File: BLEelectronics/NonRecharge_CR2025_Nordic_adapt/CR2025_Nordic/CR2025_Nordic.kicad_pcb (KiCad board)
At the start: 2 copper layers, 24 parts, among them J1 USB_A_PLUG, J2 AU-Y1006-R, Q1 Si2307CDS, U1 TPD2E2U06, U2 BAT-HLD-001, U3 LTC4412xS6, U4 LTC4054LES5-4.2#TRPBF, U5 AT25SF081-XMHD-X

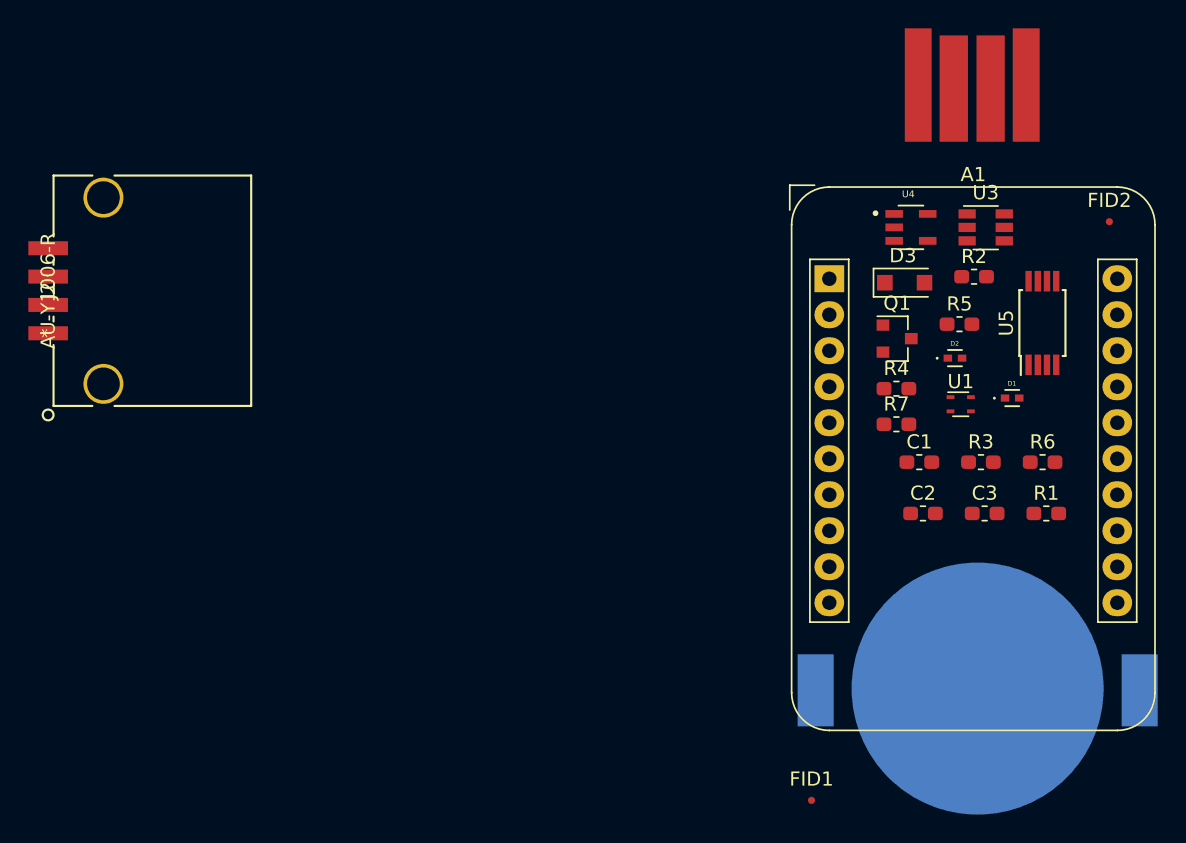
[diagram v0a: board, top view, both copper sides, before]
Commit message: added LP5970 .3V regulator to 5USB input. Created custom Nordic nRF52840 header. Todo: layout and pack libraries.
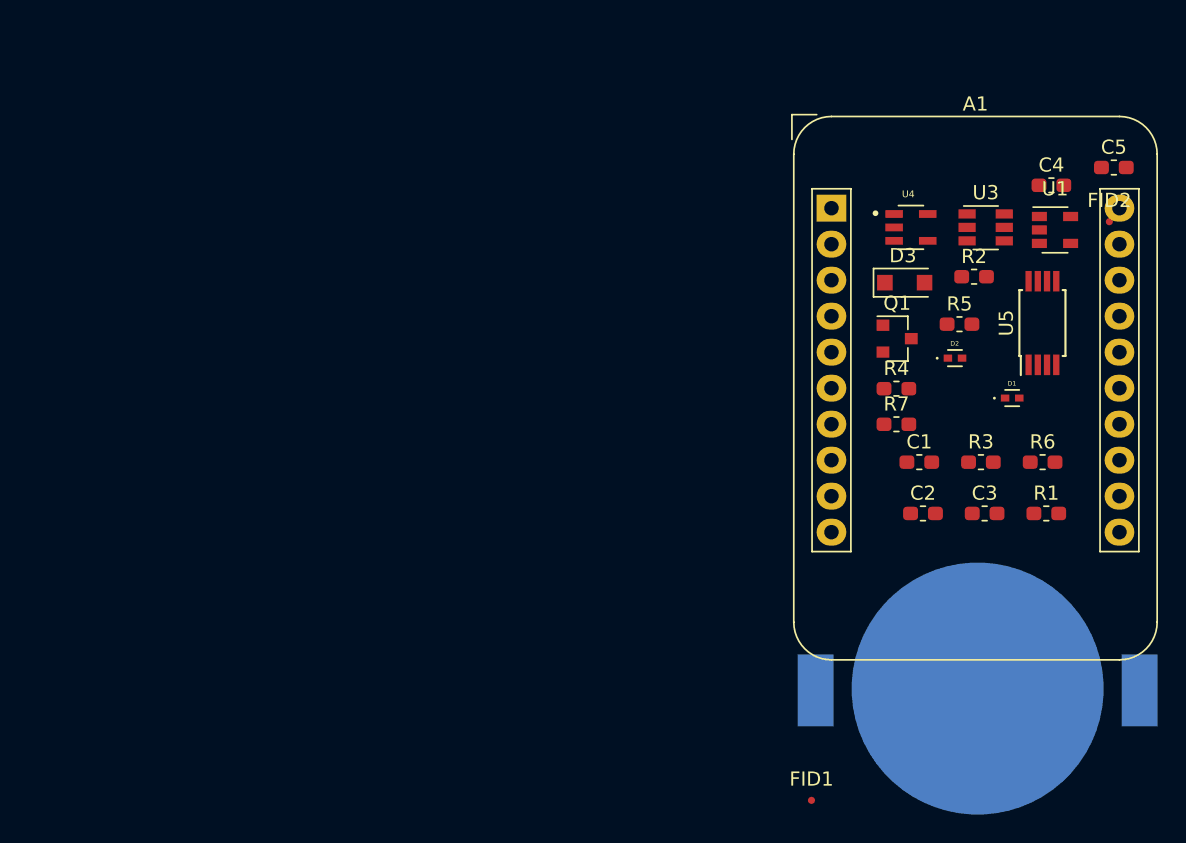
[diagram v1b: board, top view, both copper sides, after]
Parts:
- removed J1: USB_A_PLUG, 0my_footprints:usbA-PCB
- removed J2: AU-Y1006-R, 0my_footprints:AU-Y1006-R
- added C4: 1uF, Capacitor_SMD:C_0603_1608Metric_Pad1.05x0.95mm_HandSolder, F.Cu at (142.3, 77.5)
- added C5: 1uF, Capacitor_SMD:C_0603_1608Metric_Pad1.05x0.95mm_HandSolder, F.Cu at (146.7, 76.3)
- A1: value Adafruit_HUZZAH_ESP8266_breakout -> Nordic_nRF52840_breakout
- U1: value TPD2E2U06 -> LP5907MFX-3.3; footprint Package_TO_SOT_SMD:SOT-543 -> Package_TO_SOT_SMD:SOT-23-5
- U5: value AT25SF081-XMHD-X -> MX25R6435FM2IL0
- moved U1 14.0 mm to (142.6, 80.7)
- moved A1 4.98 mm to (126.8, 79.1)
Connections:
- A1 pad 11: Net-(A1-Pad11) -> GND
- A1 pad 18: Net-(A1-Pad18) -> GND
- A1 pad 19: Net-(A1-Pad19) -> /VDD_3V
- A1 pad 20: Net-(A1-Pad20) -> /5Vusb
- A1 pad 9: /3V -> Net-(A1-Pad9)
- C2 pad 1: /Vcc -> /VDD_3V
- D1 pad 2: /usbgnd -> GND
- D3 pad 1: Net-(D3-Pad1) -> Net-(C4-Pad2)
- R2 pad 1: /Vcc -> /VDD_3V
- R2 pad 2: Net-(D3-Pad1) -> Net-(C5-Pad2)
- R3 pad 1: /Vcc -> /VDD_3V
- R4 pad 1: /Vcc -> /VDD_3V
- U1 pad 1: Net-(U1-Pad1) -> Net-(C4-Pad2)
- U1 pad 3: /D- -> Net-(C4-Pad2)
- U1 pad 4: GND -> Net-(U1-Pad4)
- U5 pad 4: Net-(U5-Pad4) -> GND
- U5 pad 8: Net-(U5-Pad8) -> /VDD_3V
